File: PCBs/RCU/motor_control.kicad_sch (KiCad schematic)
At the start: 18 parts, among them U300 OPA365xxD, U301 DRV8876, U302 OPA365xxD, U303 DRV8876

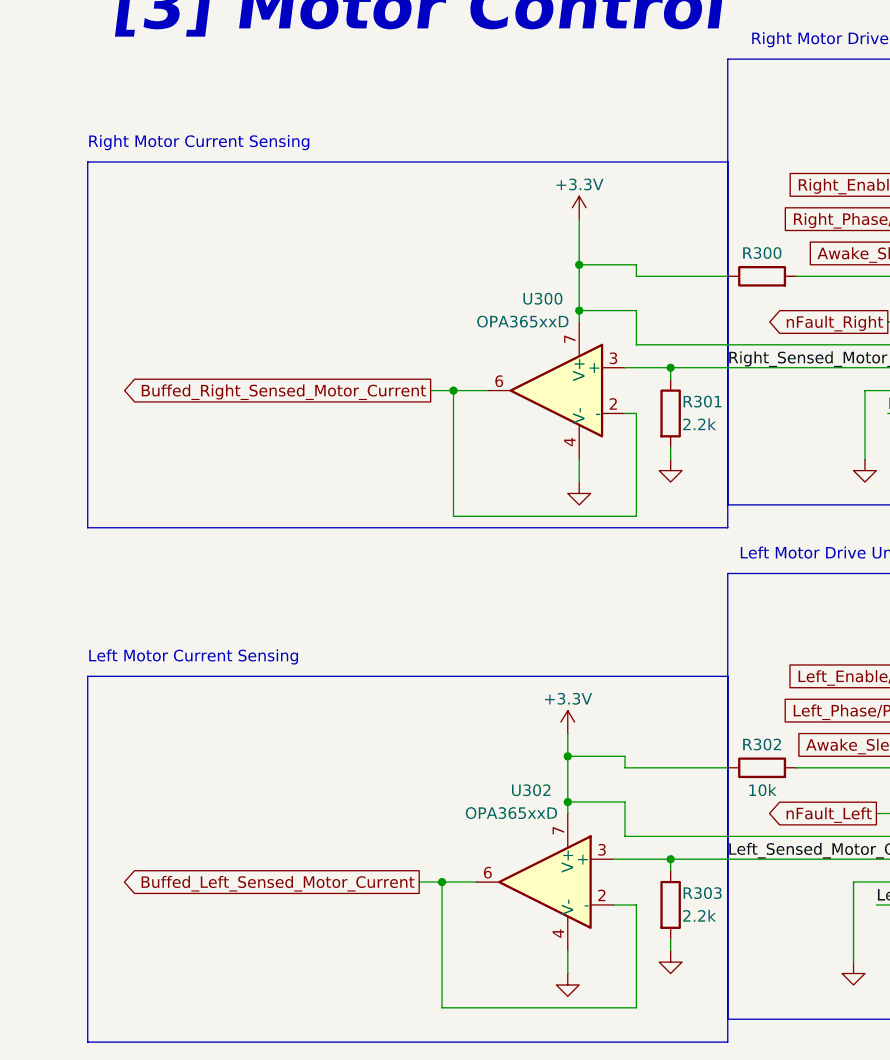
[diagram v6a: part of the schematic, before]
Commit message: Sectioned ADC module and corrected Motor current output name
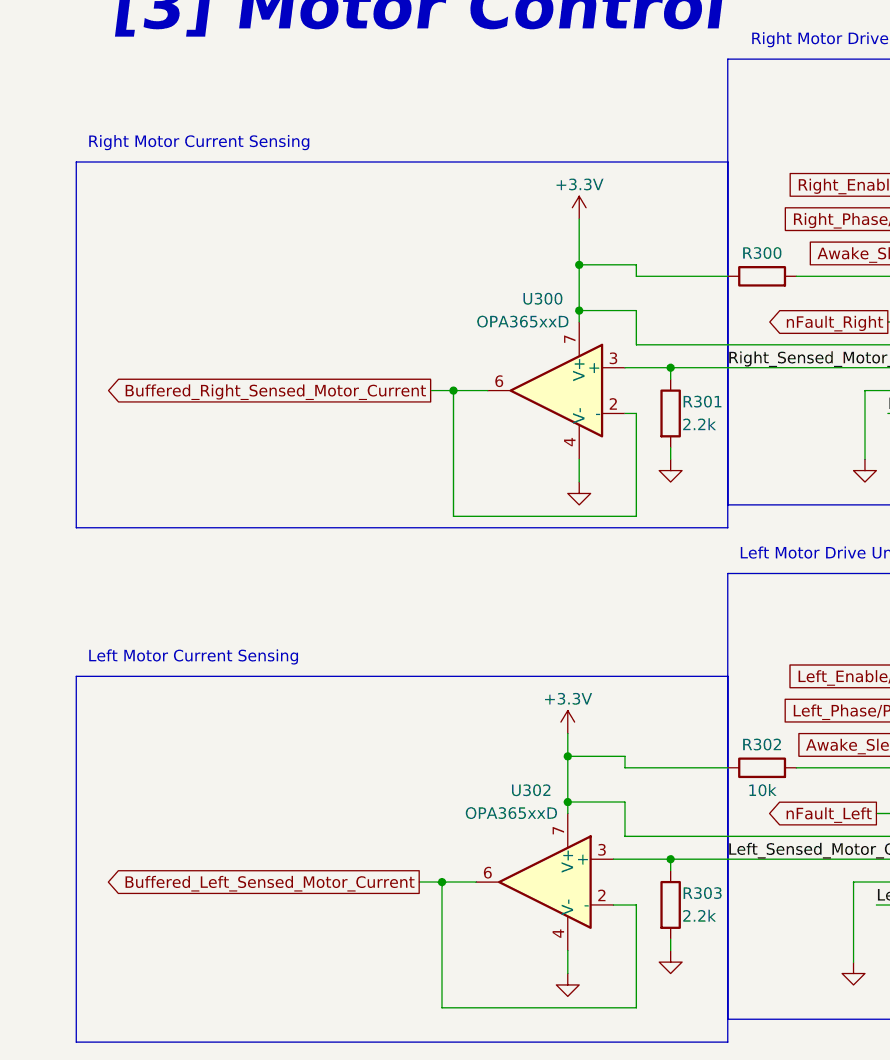
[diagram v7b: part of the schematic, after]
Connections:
- net Buffed_Left_Sensed_Motor_Current renamed Buffered_Left_Sensed_Motor_Current
- net Buffed_Right_Sensed_Motor_Current renamed Buffered_Right_Sensed_Motor_Current
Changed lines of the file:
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@@
     (stroke (width 0) (type default) (color 0 0 0 0))
   )
-  (polyline (pts (xy 15.24 97.79) (xy 86.36 97.79))
+  (polyline (pts (xy 13.97 97.79) (xy 86.36 97.79))
     (stroke (width 0) (type default) (color 0 0 0 0))
   )
@@
     (stroke (width 0) (type default) (color 0 0 0 0))
   )
-  (polyline (pts (xy 15.24 138.43) (xy 15.24 97.79))
-    (stroke (width 0) (type default) (color 0 0 0 0))
-  )
-  (polyline (pts (xy 15.24 40.64) (xy 86.36 40.64))
-    (stroke (width 0) (type default) (color 0 0 0 0))
-  )
-  (polyline (pts (xy 15.24 138.43) (xy 86.36 138.43))
+  (polyline (pts (xy 13.97 138.43) (xy 13.97 97.79))
+    (stroke (width 0) (type default) (color 0 0 0 0))
+  )
+  (polyline (pts (xy 13.97 40.64) (xy 86.36 40.64))
+    (stroke (width 0) (type default) (color 0 0 0 0))
+  )
+  (polyline (pts (xy 13.97 138.43) (xy 86.36 138.43))
     (stroke (width 0) (type default) (color 0 0 0 0))
   )
@@
     (stroke (width 0) (type default) (color 0 0 0 0))
   )
-  (polyline (pts (xy 15.24 81.28) (xy 15.24 40.64))
+  (polyline (pts (xy 13.97 81.28) (xy 13.97 40.64))
     (stroke (width 0) (type default) (color 0 0 0 0))
   )
@@
     (stroke (width 0) (type default) (color 0 0 0 0))
   )
-  (polyline (pts (xy 15.24 81.28) (xy 86.36 81.28))
+  (polyline (pts (xy 13.97 81.28) (xy 86.36 81.28))
     (stroke (width 0) (type default) (color 0 0 0 0))
   )
@@
     (effects (font (size 1.27 1.27)) (justify left bottom))
   )
-  (global_label "Buffed_Right_Sensed_Motor_Current" (shape output) (at 53.34 66.04 180) (fields_autoplaced)
-    (effects (font (size 1.27 1.27)) (justify right))
-    (property "Intersheet References" "${INTERSHEET_REFS}" (id 0) (at 17.1207 65.9606 0)
+  (global_label "Buffered_Right_Sensed_Motor_Current" (shape output) (at 53.34 66.04 180) (fields_autoplaced)
+    (effects (font (size 1.27 1.27)) (justify right))
+    (property "Intersheet References" "${INTERSHEET_REFS}" (id 0) (at 15.2459 65.9606 0)
       (effects (font (size 1.27 1.27)) (justify right) hide)
     )
@@
     )
   )
-  (global_label "Buffed_Left_Sensed_Motor_Current" (shape output) (at 52.07 120.65 180) (fields_autoplaced)
-    (effects (font (size 1.27 1.27)) (justify right))
-    (property "Intersheet References" "${INTERSHEET_REFS}" (id 0) (at 17.1812 120.5706 0)
-      (effects (font (size 1.27 1.27)) (justify right) hide)
-    )
+  (global_label "Buffered_Left_Sensed_Motor_Current" (shape output) (at 52.07 120.65 180) (fields_autoplaced)
+    (effects (font (size 1.27 1.27)) (justify right))
+    (property "Intersheet References" "${INTERSHEET_REFS}" (id 0) (at 15.3064 120.5706 0)
+      (effects (font (size 1.27 1.27)) (justify right) hide)
+    )

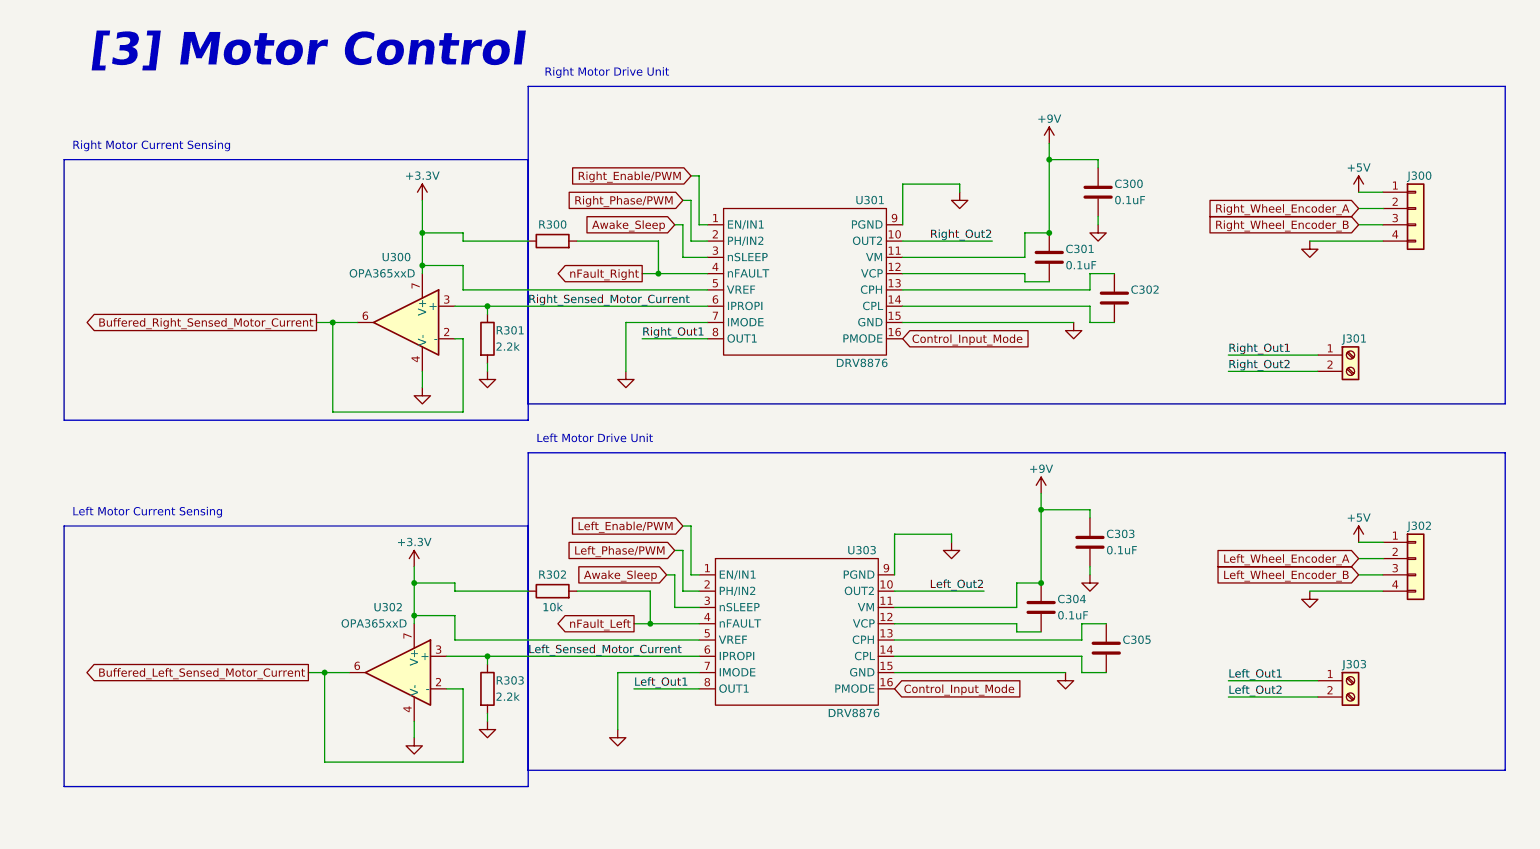
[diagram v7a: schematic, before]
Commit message: The shared SWCLK/BOOT0 pin has an internal pull-down resistor, and in the case where SWCLK is shared and are programming with SWD, just need NRST conncted to the STLink-V2 module
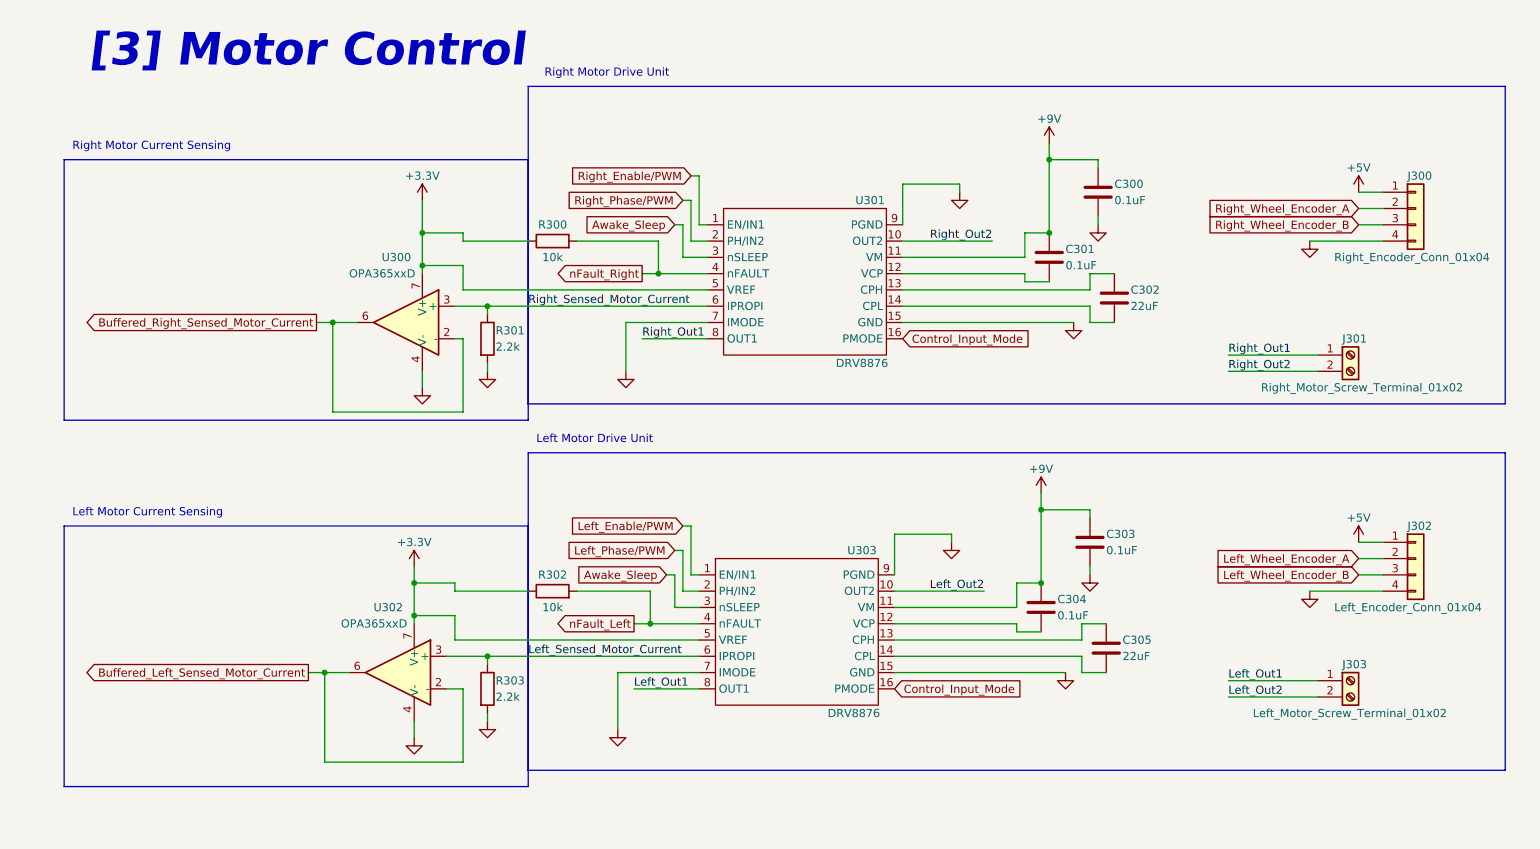
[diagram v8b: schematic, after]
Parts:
- C302, C305: value (none) -> 22uF
- J300: value (none) -> Right_Encoder_Conn_01x04
- J301: value (none) -> Right_Motor_Screw_Terminal_01x02
- J302: value (none) -> Left_Encoder_Conn_01x04
- J303: value (none) -> Left_Motor_Screw_Terminal_01x02
- R300: value (none) -> 10k
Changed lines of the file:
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@@
       (effects (font (size 1.27 1.27)) (justify left))
     )
-    (property "Value" "" (id 1) (at 200.66 76.2 0)
+    (property "Value" "Right_Motor_Screw_Terminal_01x02" (id 1) (at 200.66 76.2 0)
       (effects (font (size 1.27 1.27)) (justify left))
     )
@@
       (effects (font (size 1.27 1.27)) (justify left))
     )
-    (property "Value" "" (id 1) (at 212.09 55.88 0)
+    (property "Value" "Right_Encoder_Conn_01x04" (id 1) (at 212.09 55.88 0)
       (effects (font (size 1.27 1.27)) (justify left))
     )
@@
     (in_bom yes) (on_board yes)
     (property "Reference" "R300" (id 0) (at 90.17 50.8 90))
-    (property "Value" "" (id 1) (at 90.17 55.88 90))
+    (property "Value" "10k" (id 1) (at 90.17 55.88 90))
     (property "Footprint" "" (id 2) (at 90.17 55.118 90)
       (effects (font (size 1.27 1.27)) hide)
@@
       (effects (font (size 1.27 1.27)) (justify left))
     )
-    (property "Value" "" (id 1) (at 180.34 63.5 0)
+    (property "Value" "22uF" (id 1) (at 180.34 63.5 0)
       (effects (font (size 1.27 1.27)) (justify left))
     )
@@
       (effects (font (size 1.27 1.27)) (justify left))
     )
-    (property "Value" "" (id 1) (at 179.07 118.11 0)
+    (property "Value" "22uF" (id 1) (at 179.07 118.11 0)
       (effects (font (size 1.27 1.27)) (justify left))
     )
@@
       (effects (font (size 1.27 1.27)) (justify left))
     )
-    (property "Value" "" (id 1) (at 212.09 110.49 0)
+    (property "Value" "Left_Encoder_Conn_01x04" (id 1) (at 212.09 110.49 0)
       (effects (font (size 1.27 1.27)) (justify left))
     )
@@
       (effects (font (size 1.27 1.27)) (justify left))
     )
-    (property "Value" "" (id 1) (at 199.39 127 0)
-      (effects (font (size 1.27 1.27)) (justify left))
-    )
+    (property "Value" "Left_Motor_Screw_Terminal_01x02" (id 1) (at 199.39 127 0)
+      (effects (font (size 1.27 1.27)) (justify left))
+    )
